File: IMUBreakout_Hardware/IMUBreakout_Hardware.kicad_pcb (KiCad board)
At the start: 2 copper layers, 31.8 x 31.8 mm, 6 parts, among them U1 Razor_9DOF_Sparkfun

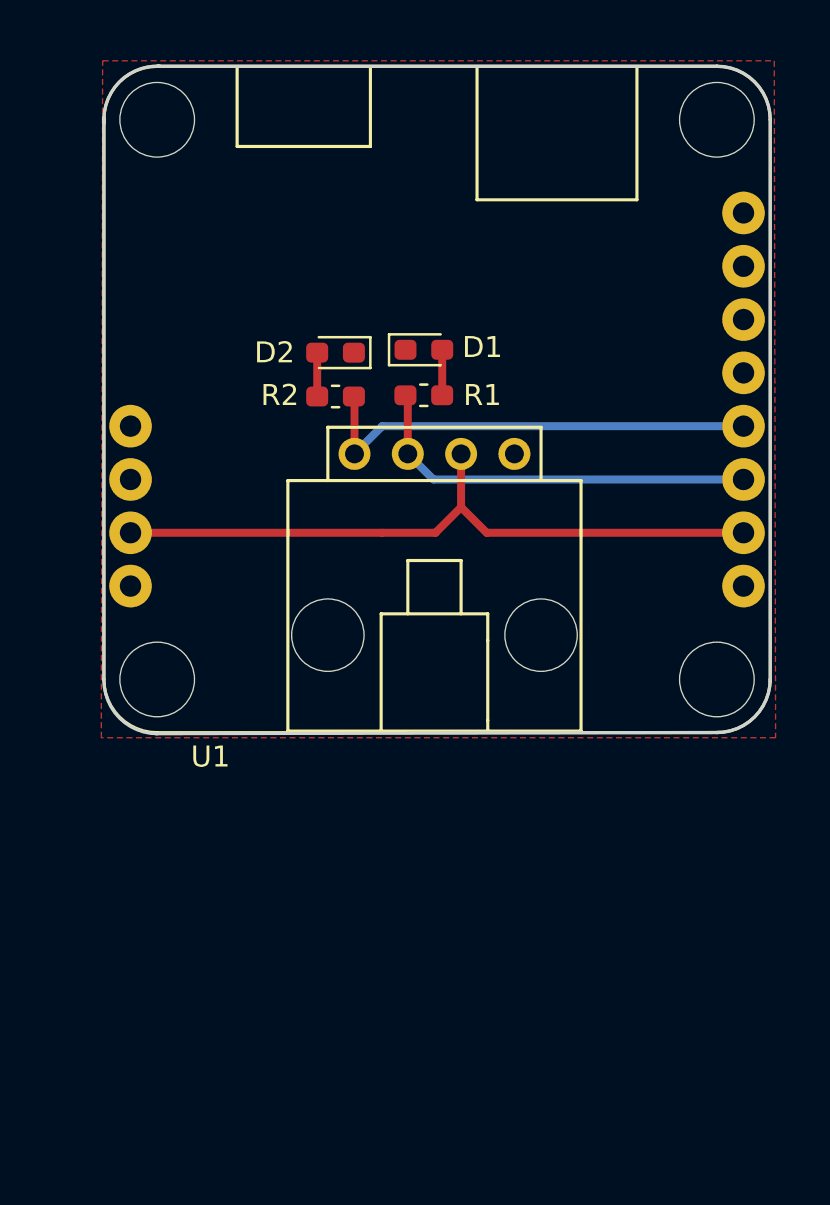
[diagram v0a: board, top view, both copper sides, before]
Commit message: Expand board, Power LED
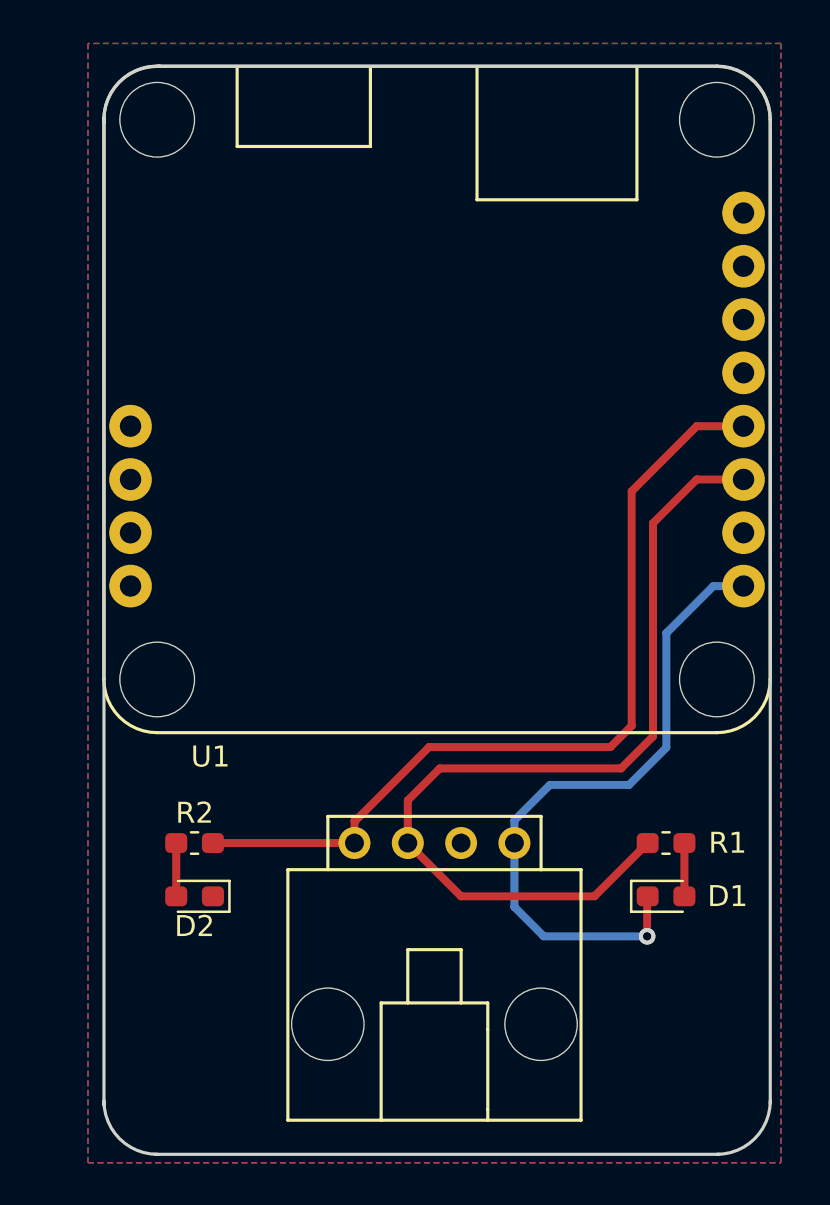
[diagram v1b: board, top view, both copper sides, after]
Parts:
- moved D1 28.5 mm to (172.3, 101.6)
- moved D2 26.8 mm to (149.9, 101.6)
- moved R1 24.3 mm to (172.3, 99.1)
- moved R2 22.3 mm to (149.9, 99.1)
- moved Conn1 18.5 mm to (161.3, 99.1)
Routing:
- net +3V3: track 32.8 -> 0.00 mm
- net GND: track 0.00 -> 31.7 mm, vias 0 -> 1
- net RX: track 19.3 -> 43.8 mm
- net TX: track 21.8 -> 40.7 mm
- added copper zone on B.Cu, net +3V3
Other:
- board size 31.8 x 31.8 mm -> 31.8 x 51.9 mm

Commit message: Made zSilkscreen edits
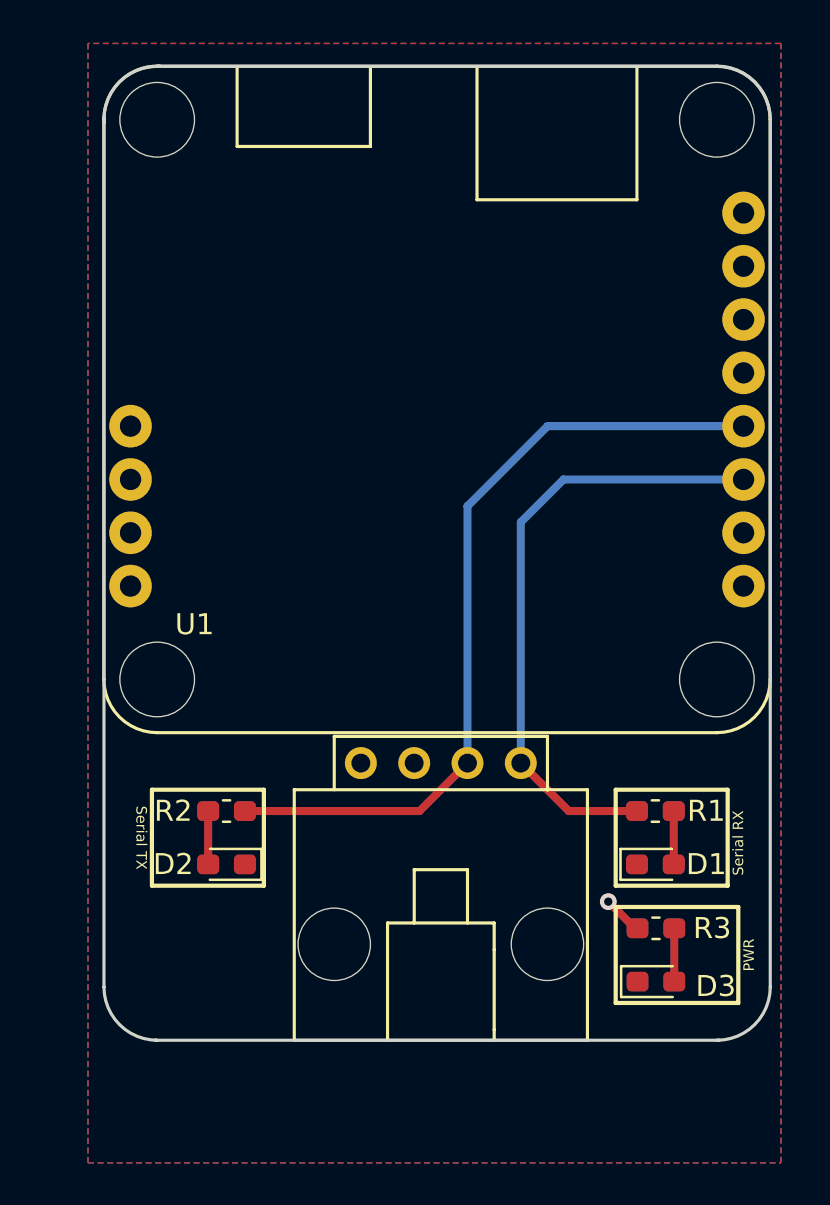
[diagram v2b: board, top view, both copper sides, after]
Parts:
- added D3: LED, LED_SMD:LED_0603_1608Metric_Pad1.05x0.95mm_HandSolder, F.Cu at (171.8, 105.7)
- added R3: 500, Resistor_SMD:R_0603_1608Metric_Pad1.05x0.95mm_HandSolder, F.Cu at (171.8, 103.1)
- moved Conn1 3.82 mm to (161.6, 95.2)
- moved D2 2.16 mm to (151.4, 100.1)
- moved R2 2.16 mm to (151.4, 97.5)
- moved D1 1.61 mm to (171.8, 100.1)
- moved R1 1.61 mm to (171.8, 97.5)
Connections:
- Conn1 pad 1: GND -> RX
- Conn1 pad 2: +3V3 -> TX
- Conn1 pad 3: RX -> GND
- Conn1 pad 4: TX -> +3V3
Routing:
- net GND: track 31.7 -> 0.04 mm, vias 1 -> 0
- net RX: track 43.8 -> 29.4 mm
- net Net-(D3-Pad2): track 0.00 -> 2.54 mm
- net TX: track 40.7 -> 38.5 mm
- net +3V3: track 0.00 -> 1.72 mm, vias 0 -> 1
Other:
- board size 31.8 x 51.9 mm -> 31.8 x 46.4 mm
- board text added: "+3V3"
- board text added: "1"
- board text added: "2"
- board text added: "3"
- board text added: "4"
- board text added: "GND"
- board text added: "PWR"
- board text added: "RX"
- board text added: "Serial RX"
- board text added: "Serial TX"
- board text added: "TX"

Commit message: edge cuts
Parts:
- moved D3 1.08 mm to (171.1, 104.9)
- moved R3 1.08 mm to (171.1, 102.4)
- moved D1 0.25 mm to (171.6, 100.1)
- moved R1 0.25 mm to (171.6, 97.5)
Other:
- outline, holes or cut-outs redrawn
- board text removed: "Serial RX"
- board text removed: "Serial TX"
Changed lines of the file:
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@@
   )
   (module LED_SMD:LED_0603_1608Metric_Pad1.05x0.95mm_HandSolder (layer F.Cu)
-    (at 171.817 100.076)
+    (at 171.563 100.076)
     (descr "LED SMD 0603 (1608 Metric), square (rectangular) end terminal, IPC_7351 nominal, (Body size source: http://www.tortai-tech.com/upload/download/2011102023233369053.pdf), generated with kicad-footprint-generator")
     (tags "LED handsolder")
@@
   )
   (module Resistor_SMD:R_0603_1608Metric_Pad1.05x0.95mm_HandSolder (layer F.Cu)
-    (at 171.817 97.536 180)
+    (at 171.563 97.536 180)
     (descr "Resistor SMD 0603 (1608 Metric), square (rectangular) end terminal, IPC_7351 nominal with elongated pad for handsoldering. (Body size source: http://www.tortai-tech.com/upload/download/2011102023233369053.pdf), generated with kicad-footprint-generator")
     (tags "resistor handsolder")
@@
   )
   (module LED_SMD:LED_0603_1608Metric_Pad1.05x0.95mm_HandSolder (layer F.Cu)
-    (at 171.845 105.664)
+    (at 171.083 104.902)
     (descr "LED SMD 0603 (1608 Metric), square (rectangular) end terminal, IPC_7351 nominal, (Body size source: http://www.tortai-tech.com/upload/download/2011102023233369053.pdf), generated with kicad-footprint-generator")
     (tags "LED handsolder")
@@
   )
   (module Resistor_SMD:R_0603_1608Metric_Pad1.05x0.95mm_HandSolder (layer F.Cu)
-    (at 171.845 103.124 180)
+    (at 171.083 102.362 180)
     (descr "Resistor SMD 0603 (1608 Metric), square (rectangular) end terminal, IPC_7351 nominal with elongated pad for handsoldering. (Body size source: http://www.tortai-tech.com/upload/download/2011102023233369053.pdf), generated with kicad-footprint-generator")
     (tags "resistor handsolder")
@@
     )
   )
+  (gr_arc (start 148.082 105.918) (end 145.542 105.918) (angle -90) (layer Edge.Cuts) (width 0.15))
+  (gr_line (start 174.752 108.458) (end 148.082 108.458) (layer Edge.Cuts) (width 0.15))
+  (gr_text TX (at 146.558 98.806 270) (layer F.SilkS)
+    (effects (font (size 1.5 1.5) (thickness 0.3)))
+  )
+  (gr_text "RX\n" (at 176.276 99.06 90) (layer F.SilkS)
+    (effects (font (size 1.5 1.5) (thickness 0.3)))
+  )
+  (gr_text PWR (at 176.276 103.632 90) (layer F.SilkS)
+    (effects (font (size 1.5 1.5) (thickness 0.3)))
+  )
   (gr_text "1\n\n" (at 164.338 92.71 270) (layer B.SilkS)
     (effects (font (size 1.5 1.5) (thickness 0.3)) (justify mirror))
@@
     (effects (font (size 1.5 1.5) (thickness 0.3)) (justify mirror))
   )
-  (gr_text "PWR\n" (at 176.276 104.394 90) (layer F.SilkS)
-    (effects (font (size 0.5 0.5) (thickness 0.1)))
-  )
-  (gr_line (start 169.926 102.108) (end 169.926 106.68) (layer F.SilkS) (width 0.2))
-  (gr_line (start 175.768 102.108) (end 169.926 102.108) (layer F.SilkS) (width 0.2))
-  (gr_line (start 175.768 106.68) (end 175.768 102.108) (layer F.SilkS) (width 0.2))
-  (gr_line (start 169.926 106.68) (end 175.768 106.68) (layer F.SilkS) (width 0.2))
-  (gr_text "Serial TX\n" (at 147.32 98.806 270) (layer F.SilkS)
-    (effects (font (size 0.5 0.5) (thickness 0.1)))
-  )
+  (gr_line (start 169.164 101.346) (end 169.164 105.918) (layer F.SilkS) (width 0.2))
+  (gr_line (start 175.006 101.346) (end 169.164 101.346) (layer F.SilkS) (width 0.2))
+  (gr_line (start 175.006 105.918) (end 175.006 101.346) (layer F.SilkS) (width 0.2))
+  (gr_line (start 169.164 105.918) (end 175.006 105.918) (layer F.SilkS) (width 0.2))
   (gr_line (start 147.828 101.092) (end 153.162 101.092) (layer F.SilkS) (width 0.2))
   (gr_line (start 147.828 96.52) (end 147.828 101.092) (layer F.SilkS) (width 0.2))
   (gr_line (start 153.162 96.52) (end 147.828 96.52) (layer F.SilkS) (width 0.2))
   (gr_line (start 153.162 101.092) (end 153.162 96.52) (layer F.SilkS) (width 0.2))
-  (gr_text "Serial RX\n" (at 175.768 99.06 90) (layer F.SilkS)
-    (effects (font (size 0.5 0.5) (thickness 0.1)))
-  )
-  (gr_line (start 175.26 96.52) (end 169.926 96.52) (layer F.SilkS) (width 0.2))
-  (gr_line (start 175.26 101.092) (end 175.26 96.52) (layer F.SilkS) (width 0.2))
-  (gr_line (start 169.926 101.092) (end 175.26 101.092) (layer F.SilkS) (width 0.2))
-  (gr_line (start 169.926 96.52) (end 169.926 101.092) (layer F.SilkS) (width 0.2))
+  (gr_line (start 175.006 96.52) (end 169.672 96.52) (layer F.SilkS) (width 0.2))
+  (gr_line (start 175.006 101.092) (end 175.006 96.52) (layer F.SilkS) (width 0.2))
+  (gr_line (start 169.672 101.092) (end 175.006 101.092) (layer F.SilkS) (width 0.2))
+  (gr_line (start 169.672 96.52) (end 169.672 101.092) (layer F.SilkS) (width 0.2))
   (gr_line (start 145.542 91.2368) (end 145.542 105.918) (layer Edge.Cuts) (width 0.15))
-  (gr_line (start 174.8536 108.458) (end 147.9804 108.458) (layer Edge.Cuts) (width 0.15))
   (gr_line (start 177.292 91.3384) (end 177.292 105.918) (layer Edge.Cuts) (width 0.15))
-  (gr_line (start 148.082 62.0395) (end 174.752 62.0395) (layer Edge.Cuts) (width 0.15))
-  (gr_arc (start 148.082 64.5795) (end 148.209 62.0395) (angle -97.04732902) (layer Edge.Cuts) (width 0.15))
-  (gr_arc (start 148.082 105.918) (end 145.542 105.918) (angle -90) (layer Edge.Cuts) (width 0.15))
+  (gr_line (start 148.0947 62.0395) (end 174.752 62.0395) (layer Edge.Cuts) (width 0.15))
+  (gr_arc (start 148.082 64.5795) (end 148.209 62.0395) (angle -91.43031918) (layer Edge.Cuts) (width 0.15))
   (gr_arc (start 174.752 105.918) (end 174.752 108.458) (angle -90) (layer Edge.Cuts) (width 0.15))
   (gr_line (start 177.292 64.5795) (end 177.292 91.3765) (layer Edge.Cuts) (width 0.15))
@@
     (arrow2b (pts (xy 134.62 127) (xy 135.746504 126.413579)))
   )
-  (segment (start 170.9166 100.1014) (end 170.942 100.076) (width 0.381) (layer F.Cu) (net 1))
-  (via (at 169.573804 101.852688) (size 0.8) (drill 0.4) (layers F.Cu B.Cu) (net 2))
-  (segment (start 170.97 103.124) (end 170.688 103.124) (width 0.381) (layer F.Cu) (net 2))
-  (segment (start 170.589804 102.868688) (end 169.573804 101.852688) (width 0.381) (layer F.Cu) (net 2))
+  (segment (start 170.6626 100.1014) (end 170.688 100.076) (width 0.381) (layer F.Cu) (net 1))
+  (via (at 168.811804 101.090688) (size 0.8) (drill 0.4) (layers F.Cu B.Cu) (net 2))
+  (segment (start 170.208 102.362) (end 169.926 102.362) (width 0.381) (layer F.Cu) (net 2))
+  (segment (start 169.827804 102.106688) (end 168.811804 101.090688) (width 0.381) (layer F.Cu) (net 2))
   (segment (start 160.5788 97.536) (end 162.8648 95.25) (width 0.381) (layer F.Cu) (net 3))
   (segment (start 152.259 97.536) (end 160.5788 97.536) (width 0.381) (layer F.Cu) (net 3))
@@
   (segment (start 166.675999 79.196001) (end 162.8648 83.0072) (width 0.381) (layer B.Cu) (net 3))
   (segment (start 167.6908 97.536) (end 165.4048 95.25) (width 0.381) (layer F.Cu) (net 4))
-  (segment (start 170.942 97.536) (end 167.6908 97.536) (width 0.381) (layer F.Cu) (net 4))
   (segment (start 176.017999 81.736001) (end 167.437999 81.736001) (width 0.381) (layer B.Cu) (net 4))
   (segment (start 165.4048 83.7692) (end 165.4048 95.25) (width 0.381) (layer B.Cu) (net 4))
   (segment (start 167.437999 81.736001) (end 165.4048 83.7692) (width 0.381) (layer B.Cu) (net 4))
-  (segment (start 172.692 100.076) (end 172.692 97.536) (width 0.381) (layer F.Cu) (net 5))
+  (segment (start 170.688 97.536) (end 167.6908 97.536) (width 0.381) (layer F.Cu) (net 4))
+  (segment (start 172.438 100.076) (end 172.438 97.536) (width 0.381) (layer F.Cu) (net 5))
   (segment (start 150.509 100.076) (end 150.509 97.536) (width 0.381) (layer F.Cu) (net 6))
-  (segment (start 172.72 105.664) (end 172.72 103.124) (width 0.381) (layer F.Cu) (net 13))
+  (segment (start 171.958 104.902) (end 171.958 102.362) (width 0.381) (layer F.Cu) (net 13))
   (zone (net 1) (net_name GND) (layer F.Cu) (hatch edge 0.508)
     (connect_pads yes (clearance 0.508))

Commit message: Edge cuts done
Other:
- board size 31.8 x 46.4 mm -> 31.8 x 46.6 mm
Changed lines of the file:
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@@
   (general
     (thickness 1.6)
-    (drawings 35)
+    (drawings 31)
     (tracks 17)
     (zones 0)
@@
   )
   (setup
-    (last_trace_width 0.381)
+    (last_trace_width 0.25)
     (user_trace_width 0.381)
     (trace_clearance 0.2)
@@
     )
   )
-  (gr_arc (start 148.082 105.918) (end 145.542 105.918) (angle -90) (layer Edge.Cuts) (width 0.15))
-  (gr_line (start 174.752 108.458) (end 148.082 108.458) (layer Edge.Cuts) (width 0.15))
+  (gr_line (start 177.2666 108.6612) (end 177.292 64.6049) (layer Edge.Cuts) (width 0.15))
+  (gr_line (start 145.5674 108.6612) (end 177.2666 108.6612) (layer Edge.Cuts) (width 0.15))
+  (gr_arc (start 174.752 64.5922) (end 177.292 64.5922) (angle -87.13759477) (layer Edge.Cuts) (width 0.15))
+  (gr_line (start 148.1074 62.0522) (end 174.8536 62.0522) (layer Edge.Cuts) (width 0.15))
+  (gr_arc (start 148.082 64.5922) (end 148.082 62.0522) (angle -87.13759477) (layer Edge.Cuts) (width 0.15))
+  (gr_line (start 145.542 64.4906) (end 145.5674 108.6612) (layer Edge.Cuts) (width 0.15))
   (gr_text TX (at 146.558 98.806 270) (layer F.SilkS)
     (effects (font (size 1.5 1.5) (thickness 0.3)))
@@
   (gr_line (start 169.672 101.092) (end 175.006 101.092) (layer F.SilkS) (width 0.2))
   (gr_line (start 169.672 96.52) (end 169.672 101.092) (layer F.SilkS) (width 0.2))
-  (gr_line (start 145.542 91.2368) (end 145.542 105.918) (layer Edge.Cuts) (width 0.15))
-  (gr_line (start 177.292 91.3384) (end 177.292 105.918) (layer Edge.Cuts) (width 0.15))
-  (gr_line (start 148.0947 62.0395) (end 174.752 62.0395) (layer Edge.Cuts) (width 0.15))
-  (gr_arc (start 148.082 64.5795) (end 148.209 62.0395) (angle -91.43031918) (layer Edge.Cuts) (width 0.15))
-  (gr_arc (start 174.752 105.918) (end 174.752 108.458) (angle -90) (layer Edge.Cuts) (width 0.15))
-  (gr_line (start 177.292 64.5795) (end 177.292 91.3765) (layer Edge.Cuts) (width 0.15))
-  (gr_arc (start 174.752 64.5795) (end 177.292 64.5795) (angle -90) (layer Edge.Cuts) (width 0.15))
-  (gr_line (start 145.542 64.516) (end 145.542 91.2495) (layer Edge.Cuts) (width 0.15))
   (dimension 25.4 (width 0.3) (layer F.Fab)
     (gr_text "1.0000 in" (at 107.12 99.06 90) (layer F.Fab)
@@
     (polygon
       (pts
-        (xy 144.78 114.3) (xy 177.8 114.3) (xy 177.8 60.96) (xy 144.78 60.96)
+        (xy 144.78 114.2746) (xy 177.8 114.2746) (xy 177.8 60.96) (xy 144.78 60.96)
       )
     )

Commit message: logos and signature added
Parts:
- added G***: LOGO, MRDT_Silkscreens:z_sig_Andrea_Biasella_22mmx9.3mm, F.Cu at (160.8, 82.0)
- added G***: LOGO, MRDT_Silkscreens:0_MRDT_Logo_7.5mm, F.Cu at (150.4, 104.7)
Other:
- board text added: "IMU Breakout Board, Rev1 Mars Rover Design Team Missouri S&T, 2019 Andrea Biasella"

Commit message: silkscreeens
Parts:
- added G***: LOGO, MRDT_Silkscreens:2_Dahlbot_2.0, B.Cu at (150.2, 73.5)
- moved G*** 10.3 mm to (171.0, 80.7), turned to 270 degrees
